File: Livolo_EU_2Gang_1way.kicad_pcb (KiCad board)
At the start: 2 copper layers, 43 x 43 mm, 40 parts, among them IC1 ATMEGA328P, U1 ATSHA204A, U2 RFM69_MINIMAL

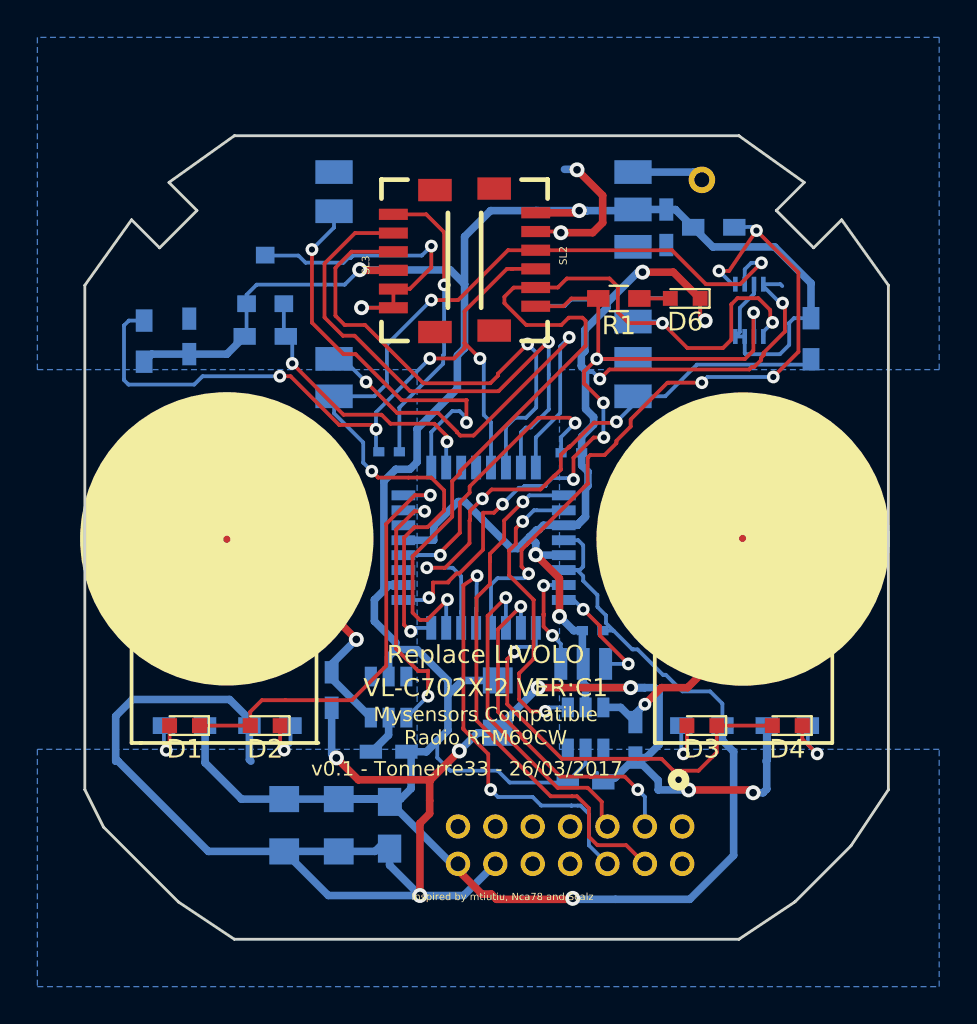
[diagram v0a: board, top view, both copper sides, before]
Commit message: optimise position C2
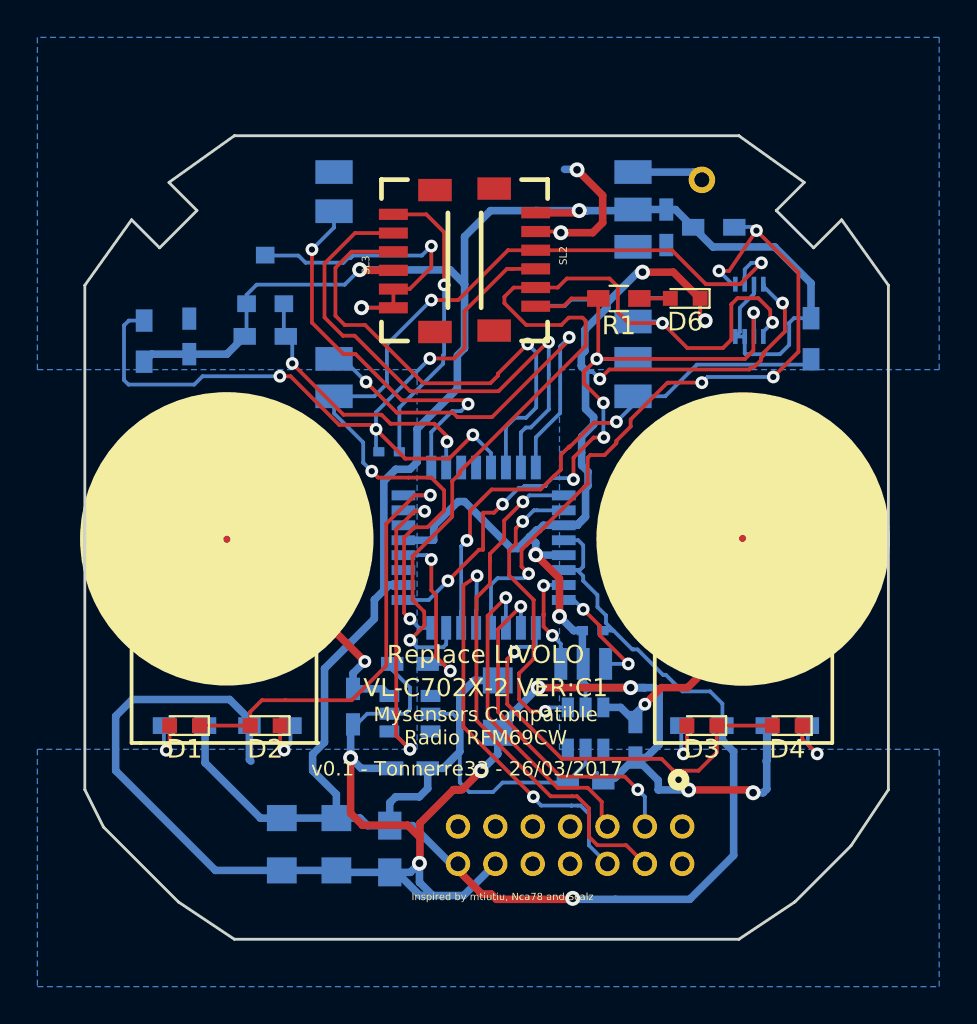
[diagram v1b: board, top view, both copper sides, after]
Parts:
- C2: footprint Capacitors_SMD:C_0402 -> Capacitors_SMD:C_0603_HandSoldering
- moved C2 14.2 mm to (144.4, 111.8), turned to 0 degrees
- moved C9 1.45 mm to (144.4, 117.4)
- moved U$6 1.45 mm to (144.4, 114.4), turned to 0 degrees
- moved C8 1.44 mm to (141.4, 114.1)
- moved C13 1.27 mm to (143.3, 121.7)
- moved C11 1.02 mm to (140.5, 121.4)
- moved C12 1.02 mm to (137.5, 121.4)
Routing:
- net Net-(C2-Pad2): track 17.5 -> 9.39 mm
- net VCC: track 173.6 -> 178.8 mm
- net /CSN: track 31.9 -> 29.8 mm, vias 3 -> 2
- net /TOUCH_2: track 14.7 -> 16.7 mm
- net /RST: track 41.4 -> 42.7 mm
- net /A2: track 22.3 -> 21.2 mm
- net /L1_SET: track 24.1 -> 23.1 mm
- net /MOSI: track 51.6 -> 52.7 mm
- net /IRQ: track 24.3 -> 23.4 mm
- net /MISO: track 49.7 -> 49.2 mm

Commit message: capacitor added for OTA
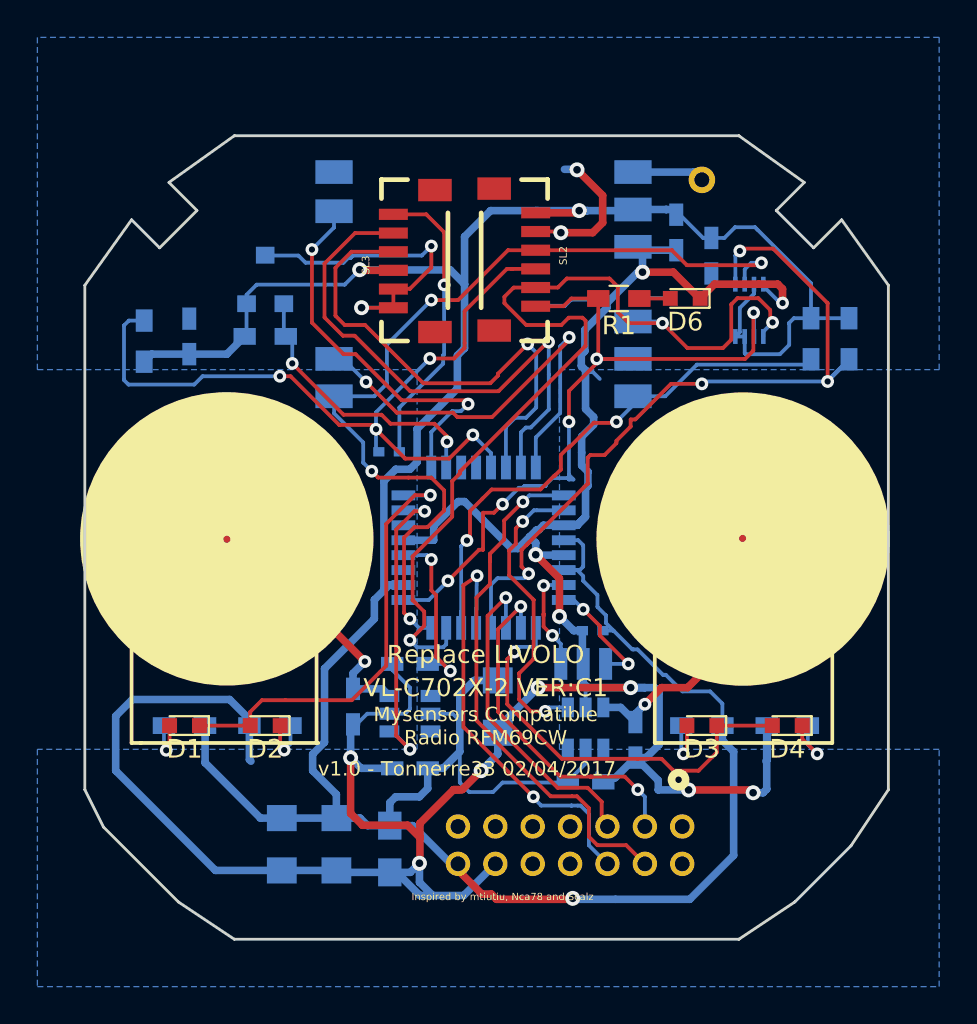
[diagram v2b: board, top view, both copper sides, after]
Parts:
- added C14: 100n, Capacitors_SMD:C_0603_HandSoldering, B.Cu at (160.5, 89.9)
- R3: value 10k -> 56k
- moved R10 9.38 mm to (167.9, 94.4), turned to 270 degrees
- moved C3 0.60 mm to (158.6, 88.7)
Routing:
- net GND: track 188.1 -> 182.2 mm, vias 17 -> 15
- net /FLASH_CS: track 39.5 -> 42.8 mm, vias 5 -> 4
- net VCC: track 178.8 -> 181.1 mm
- net /SCK: track 41.8 -> 40.8 mm, vias 7 -> 5
- net /MISO: track 49.2 -> 48.4 mm
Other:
- board text added: "v1.0 - Tonnerre33 02/04/2017"
- board text removed: "v0.1 - Tonnerre33 - 26/03/2017"

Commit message: Text cleaning and Readme update
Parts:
- U$7: value RFM12B_ANTENNA -> ANT
- U2: value RFM69_MINIMAL -> RFM69CW
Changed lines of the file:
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@@
   (page A4)
   (layers
-    (0 Top signal)
-    (31 Bottom signal)
+    (0 Top signal hide)
+    (31 Bottom signal hide)
     (32 B.Adhes user)
     (33 F.Adhes user)
@@
     (aux_axis_origin 127 126.5)
     (grid_origin 127 126.5)
-    (visible_elements 7FFFFFFF)
+    (visible_elements 7FFFFDFF)
     (pcbplotparams
       (layerselection 0x010fc_80000001)
@@
       (effects (font (size 0.8128 0.8128) (thickness 0.15)) (justify mirror))
     )
-    (fp_text value RFM12B_ANTENNA (at -2.1326 0.1052 180) (layer B.SilkS)
+    (fp_text value ANT (at -2.285 -0.2504 180) (layer B.SilkS)
       (effects (font (size 0.8128 0.8128) (thickness 0.15)) (justify mirror))
     )
@@
       (effects (font (size 1.27 1.27) (thickness 0.2032)) (justify mirror))
     )
-    (fp_text value RFM69_MINIMAL (at 0.8636 6.9342) (layer B.SilkS)
+    (fp_text value RFM69CW (at 0.8636 6.9342) (layer B.SilkS)
       (effects (font (size 0.8128 0.8128) (thickness 0.2032)) (justify mirror))
     )
@@
   (segment (start 163.322 91.567) (end 164.211 92.456) (width 0.2032) (layer Bottom) (net 1) (status 80000))
   (segment (start 163.068 91.448) (end 160.693 91.448) (width 0.4064) (layer Top) (net 1))
-  (segment (start 160.693 91.448) (end 159.931 92.21) (width 0.4064) (layer Top) (net 1) (status 800000))
+  (segment (start 160.693 91.448) (end 159.931 92.21) (width 0.4064) (layer Top) (net 1))
   (segment (start 164.338 91.702) (end 164.338 92.456) (width 0.4064) (layer Top) (net 1))
   (segment (start 164.084 91.448) (end 164.338 91.702) (width 0.4064) (layer Top) (net 1))
@@
   (segment (start 135.806 116.891) (end 135.89 116.975) (width 0.4064) (layer Bottom) (net 1))
   (segment (start 154.4168 117.9148) (end 154.4168 117.5948) (width 0.2032) (layer Bottom) (net 1))
-  (segment (start 160.528 88.974) (end 161.224 88.974) (width 0.2032) (layer Bottom) (net 2) (status 400000))
+  (segment (start 160.528 88.974) (end 161.224 88.974) (width 0.2032) (layer Bottom) (net 2))
   (segment (start 165.862 91.3972) (end 162.9918 88.527) (width 0.2032) (layer Bottom) (net 2))
   (segment (start 165.862 91.3972) (end 165.862 93.269) (width 0.2032) (layer Bottom) (net 2))

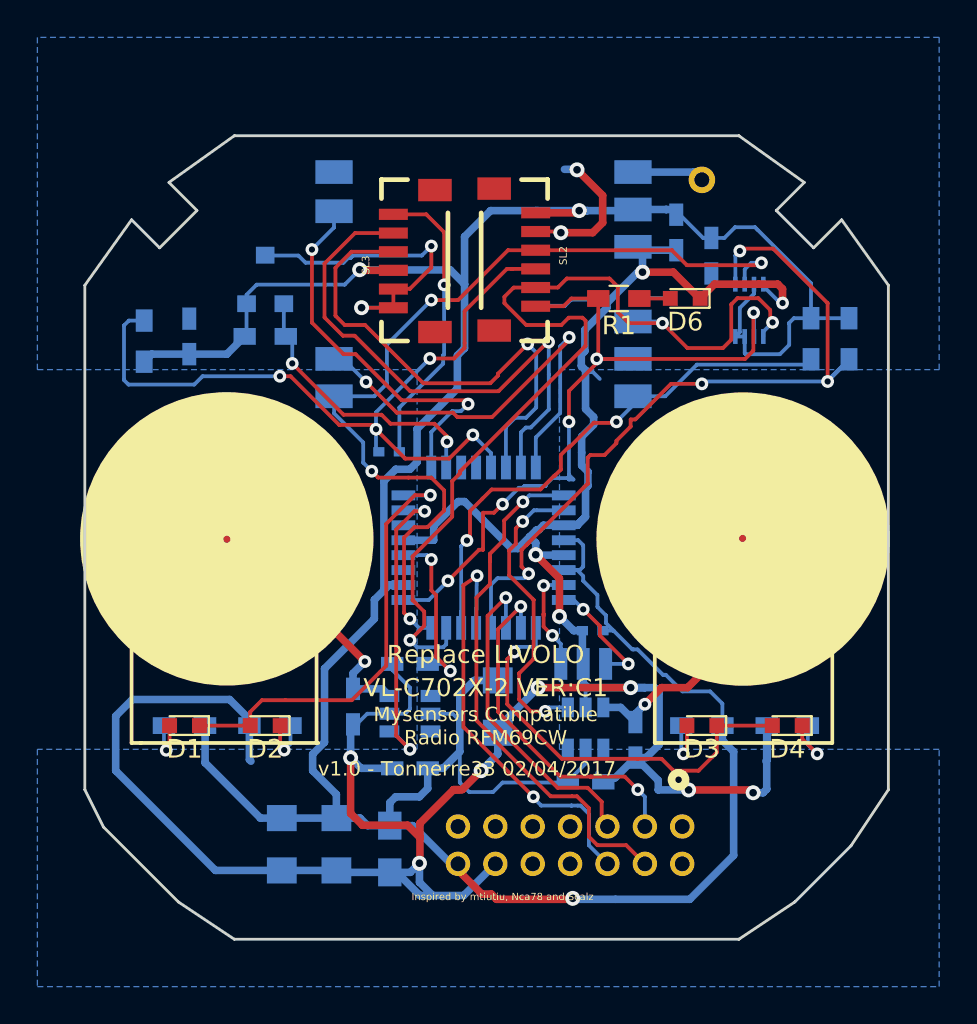
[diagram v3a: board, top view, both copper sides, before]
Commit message: power node by 12Vcc
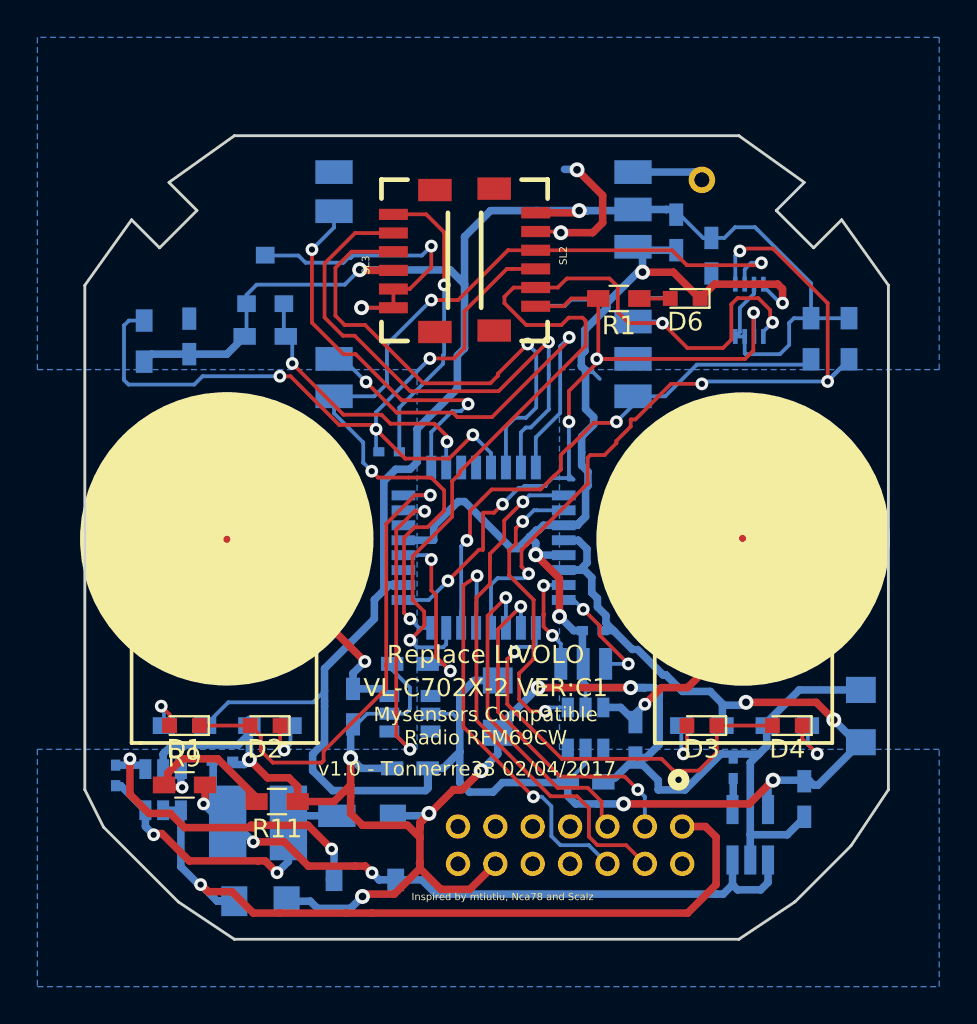
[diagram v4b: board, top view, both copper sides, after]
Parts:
- added C15: 470p, Capacitors_SMD:C_0402, B.Cu at (161.7, 117.4)
- added C16: 100n, Capacitors_SMD:C_0402, B.Cu at (128.7, 117.7)
- added C17: 22u, Capacitors_SMD:C_0402, B.Cu at (134.4, 117.0)
- added D5: SS14M, Livolo:SS14M, B.Cu at (142.0, 119.9)
- added D7: 1N4148, Diodes_SMD:D_SOD-123, B.Cu at (142.0, 123.3)
- added L1: 15uH, Livolo:VLCF4020T-150MR68, B.Cu at (136.1, 120.3)
- added R11: 10k, Resistors_SMD:R_0603_HandSoldering, F.Cu at (137.3, 119.1)
- added R9: 31k6, Resistors_SMD:R_0603_HandSoldering, F.Cu at (132.3, 118.2)
- added U3: MIC5205-3.3, TO_SOT_Packages_SMD:SOT-23-5_HandSoldering, B.Cu at (162.6, 120.9)
- added U4: MCP16301, TO_SOT_Packages_SMD:SOT-23-6, B.Cu at (131.2, 118.5)
- C10: value 10u -> 100u
- C11: value 100u -> 10u/25v
- C13: footprint Capacitors_SMD:C_0805_HandSoldering -> Capacitors_SMD:C_0603_HandSoldering
- moved C12 31.7 mm to (168.5, 114.6), turned to 270 degrees
- moved C13 22.3 mm to (165.5, 119.0)
- moved C11 5.08 mm to (136.4, 124.5), turned to 180 degrees
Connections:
- C11 pad +: VCC -> /+12VCC
- U$2 pad 13: (no net) -> /+12VCC
- U$2 pad 2: VCC -> (no net)
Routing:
- net /+12VCC: track 0.00 -> 41.9 mm, vias 0 -> 1
- net /3VCC_1: track 0.00 -> 39.6 mm, vias 0 -> 3
- net Net-(C16-Pad1): track 0.00 -> 19.0 mm, vias 0 -> 2
- net Net-(C16-Pad2): track 0.00 -> 18.0 mm, vias 0 -> 2
- net Net-(R11-Pad2): track 0.00 -> 8.88 mm, vias 0 -> 1
- net GND: track 182.2 -> 186.5 mm
- net VCC: track 181.1 -> 178.0 mm, vias 3 -> 6
- net /LED1: track 23.8 -> 26.5 mm
- net Net-(C15-Pad2): track 0.00 -> 1.67 mm

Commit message: increase clearance netclass POWER from 8 to 10 mil
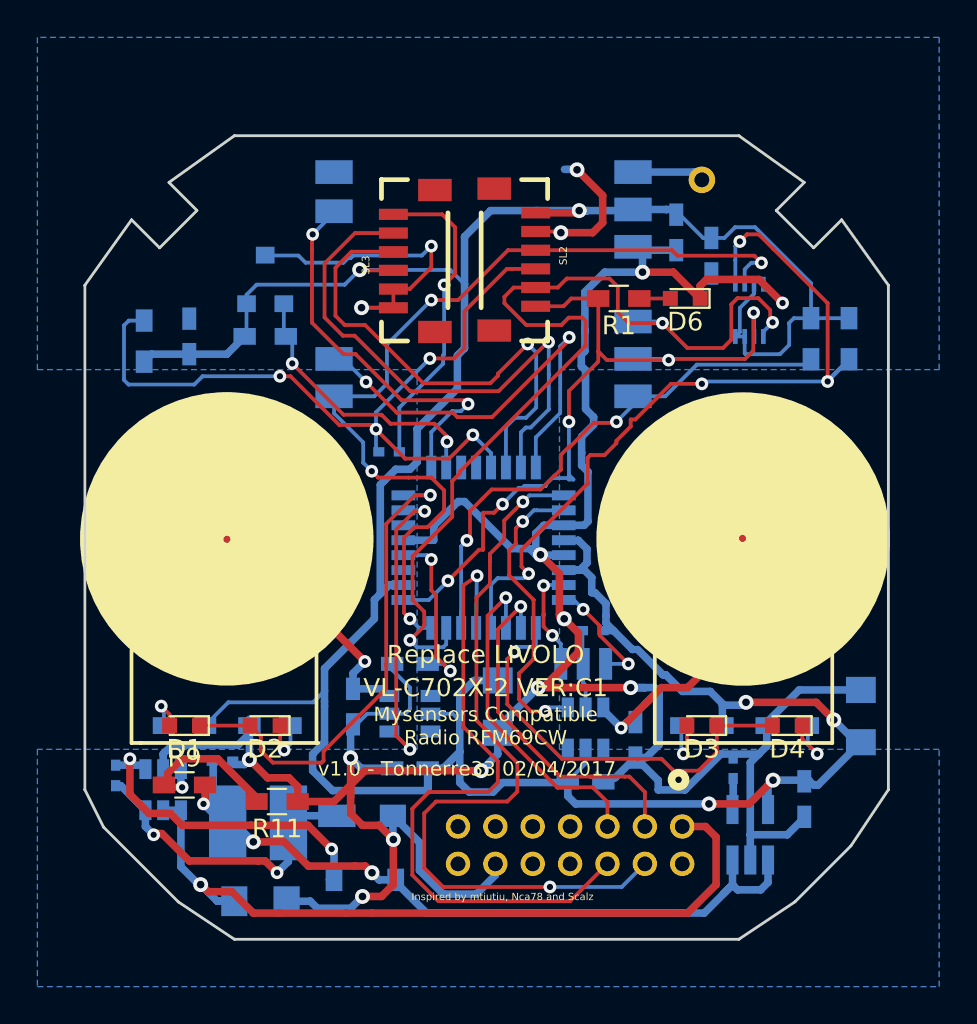
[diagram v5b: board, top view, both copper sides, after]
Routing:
- net /L1_SET: track 22.9 -> 35.7 mm, vias 2 -> 1
- net /L1_RST: track 28.4 -> 41.1 mm, vias 1 -> 2
- net GND: track 186.5 -> 192.1 mm
- net (no net): track 5.10 -> 0.00 mm
- net Net-(C4-Pad2): track 19.3 -> 20.8 mm
- net /3VCC_1: track 39.6 -> 41.0 mm
- net /DTR: track 15.9 -> 16.8 mm
- net /FLASH_CS: track 42.8 -> 43.7 mm
- net /L2_SET: track 19.1 -> 19.0 mm, vias 2 -> 1
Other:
- net class Power: clearance 0.2032 -> 0.254

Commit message: cleaning
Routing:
- net GND: track 192.1 -> 204.2 mm
- net /SCK: track 41.0 -> 39.9 mm
